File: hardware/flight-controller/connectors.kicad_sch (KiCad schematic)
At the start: 40 parts, among them J10 IDC-10, J3 IDC-10, J4 Conn_01x03, J5 Conn_01x03, J6 Conn_01x03, J7 IDC-10, J8 XT-60, J9 Conn_01x03

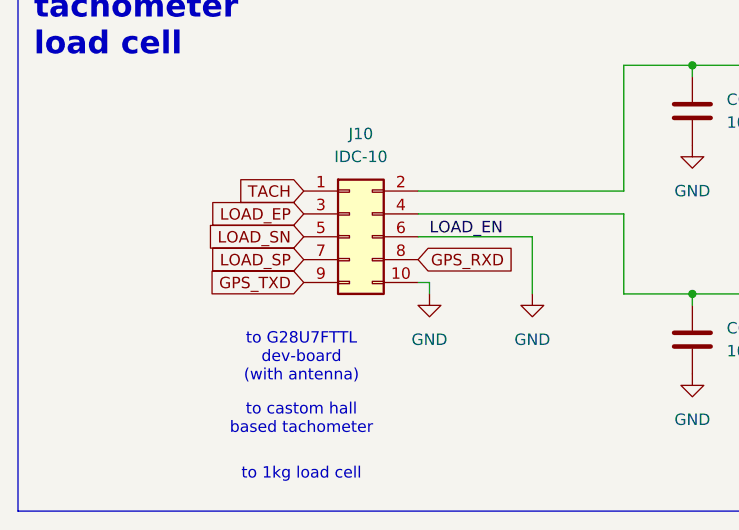
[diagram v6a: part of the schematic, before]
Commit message: fix connector GPS pinout, update AUX pinouts
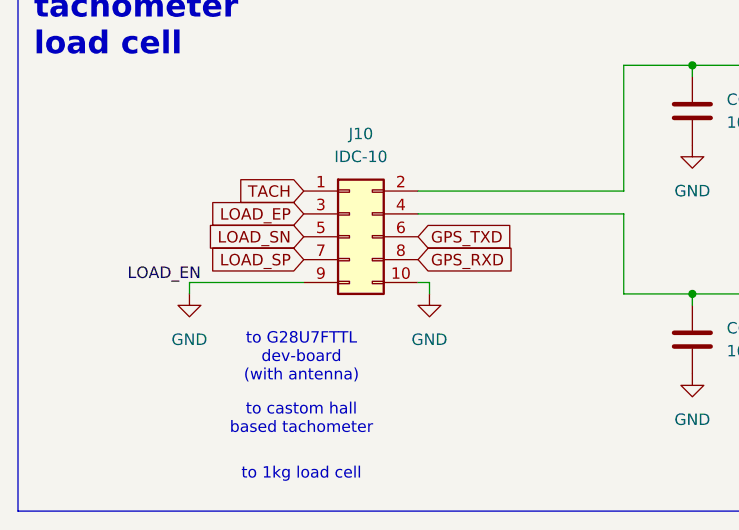
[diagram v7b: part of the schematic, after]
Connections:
- net GND: now also J10.9 (Pin_9); no longer J10.6 (Pin_6)
- net GPS_TXD: now also J10.6 (Pin_6); no longer J10.9 (Pin_9)
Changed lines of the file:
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@@
 	(wire
 		(pts
-			(xy 63.5 161.29) (xy 76.2 161.29)
-		)
-		(stroke
-			(width 0)
-			(type default)
-		)
-	)
-	(wire
-		(pts
 			(xy 55.88 102.87) (xy 81.28 102.87)
 		)
@@
 	(wire
 		(pts
-			(xy 151.13 167.64) (xy 153.67 167.64)
+			(xy 50.8 166.37) (xy 38.1 166.37)
 		)
 		(stroke
@@
 	(wire
 		(pts
-			(xy 76.2 167.64) (xy 76.2 161.29)
+			(xy 151.13 167.64) (xy 153.67 167.64)
 		)
 		(stroke
@@
 	(wire
 		(pts
+			(xy 38.1 166.37) (xy 38.1 167.64)
+		)
+		(stroke
+			(width 0)
+			(type default)
+		)
+	)
+	(wire
+		(pts
 			(xy 63.5 158.75) (xy 86.36 158.75)
 		)
@@
 	)
 	(label "LOAD_EN"
-		(at 64.77 161.29 0)
+		(at 39.37 166.37 180)
 		(fields_autoplaced yes)
 		(effects
@@
 				(size 1.27 1.27)
 			)
-			(justify left bottom)
+			(justify right bottom)
 		)
 	)
@@
 	(global_label "GPS_TXD"
 		(shape input)
-		(at 50.8 166.37 180)
+		(at 63.5 161.29 0)
 		(fields_autoplaced yes)
 		(effects
@@
 				(size 1.27 1.27)
 			)
-			(justify right)
+			(justify left)
 		)
 		(property "Intersheetrefs" "${INTERSHEET_REFS}"
-			(at 39.6506 166.37 0)
+			(at 74.6494 161.29 0)
 			(effects
 				(font
 					(size 1.27 1.27)
 				)
-				(justify right)
+				(justify left)
 				(hide yes)
 			)
@@
 	(symbol
 		(lib_id "power:GND")
-		(at 76.2 167.64 0)
+		(at 38.1 167.64 0)
 		(mirror y)
 		(unit 1)
@@
 		(dnp no)
 		(property "Reference" "#PWR0128"
-			(at 76.2 173.99 0)
+			(at 38.1 173.99 0)
 			(effects
 				(font
@@
 		)
 		(property "Value" "GND"
-			(at 76.2 172.72 0)
+			(at 38.1 172.72 0)
 			(effects
 				(font
@@
 		)
 		(property "Footprint" ""
-			(at 76.2 167.64 0)
+			(at 38.1 167.64 0)
 			(effects
 				(font
@@
 		)
 		(property "Datasheet" ""
-			(at 76.2 167.64 0)
+			(at 38.1 167.64 0)
 			(effects
 				(font
@@
 		)
 		(property "Description" "Power symbol creates a global label with name \"GND\" , ground"
-			(at 76.2 167.64 0)
+			(at 38.1 167.64 0)
 			(effects
 				(font
